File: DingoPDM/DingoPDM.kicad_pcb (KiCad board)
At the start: 4 copper layers, 71.1 x 88.9 mm, 112 parts, among them J1 RedCubeTerminal, J2 RedCubeTerminal, J3 Conn_01x12, J4 TC, U1 VXO780x-500-M, U11 BTS7008-2EPA, U12 BTS724G, U2 LD1117S33CTR, U3 PCA82C250, U4 STM32F303CCTx, U5 MB85RC256V, U6 MCP9808, U7 LM324, U8 BTS700n-1EPP, U9 BTS700n-1EPP, Y1 8mHz

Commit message: Added documentation, finished and cleaned design
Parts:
- moved G1 61.4 mm to (30.0, 32.4)
- moved TP1 23.4 mm to (-34.2, -15.6)
- moved H3 11.9 mm to (-21.1, -21.6)
- moved J2 8.33 mm to (-30.5, -23.9)
- moved C7 1.17 mm to (0.97, 49.3)
- moved C8 1.12 mm to (4.67, 49.3)
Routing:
- net GND: track 51.7 -> 72.2 mm, vias 50 -> 52
- net +5V: track 171.8 -> 157.9 mm
- net INPUT2: track 43.1 -> 46.3 mm
- net INPUT1: track 39.9 -> 41.6 mm
- net PF_IN5: track 112.2 -> 113.5 mm
- net PF_ST5_6: track 110.7 -> 111.6 mm
- added copper zone on In1.Cu, net GND
- removed copper zone on In2.Cu, net GND
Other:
- board size 71.1 x 88.9 mm -> 71.1 x 82.5 mm

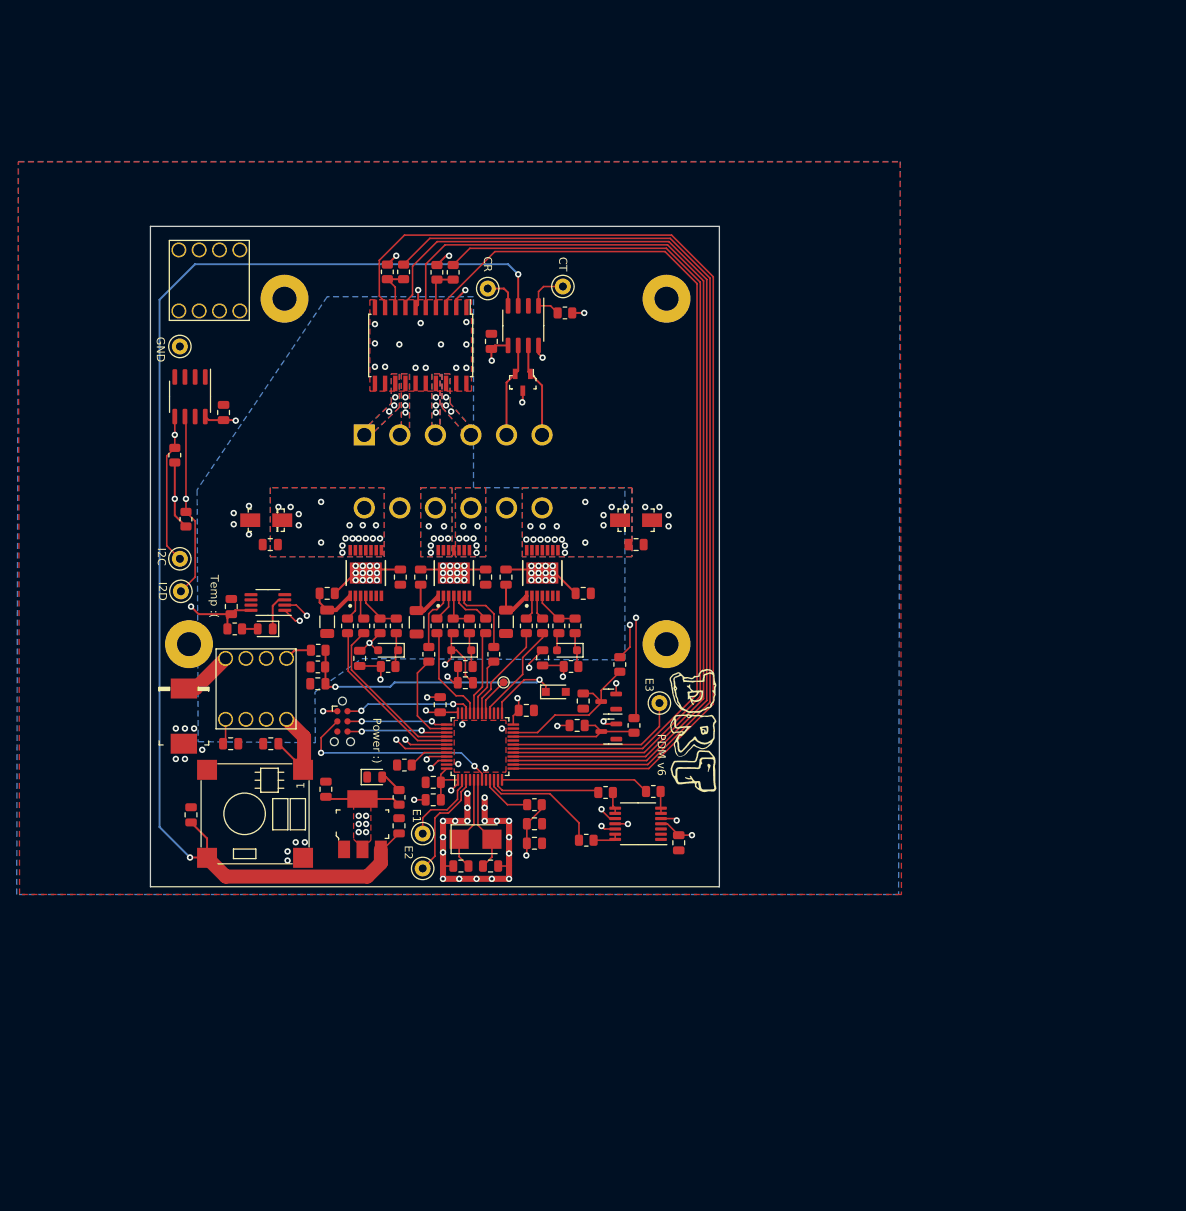
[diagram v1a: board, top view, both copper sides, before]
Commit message: Changed to STM32F446RE
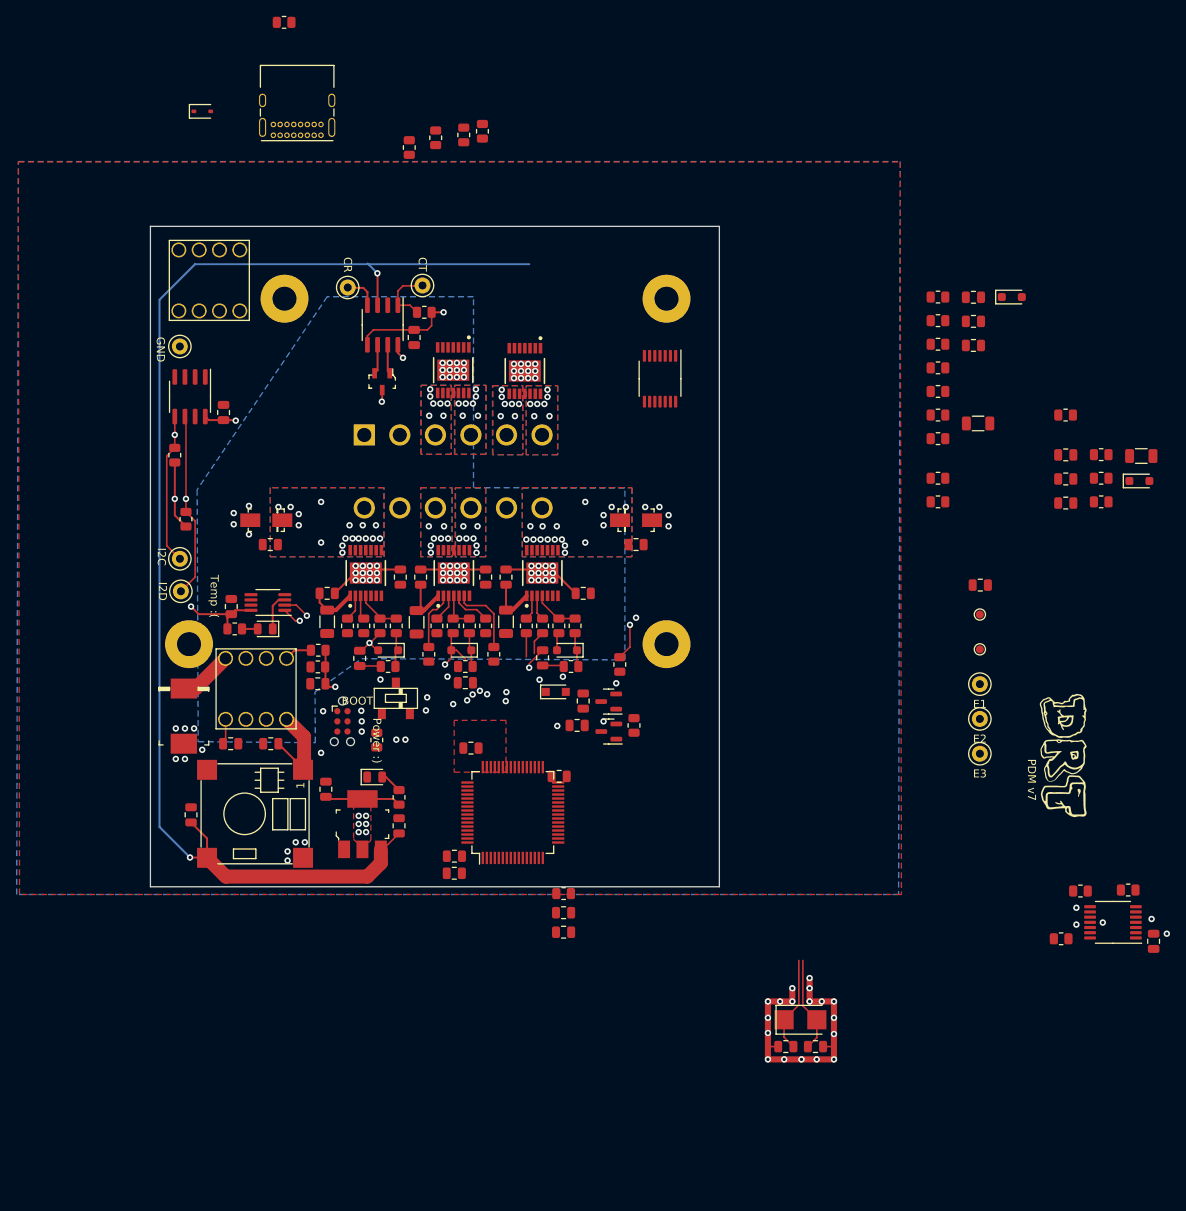
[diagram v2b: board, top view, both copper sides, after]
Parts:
- added C10: 47nF, Capacitor_SMD:C_0805_2012Metric, F.Cu at (76.6, -2.07)
- added C33: 100nF, Capacitor_SMD:C_0805_2012Metric, F.Cu at (76.6, 0.94)
- added C34: 220pF, Capacitor_SMD:C_0805_2012Metric, F.Cu at (76.6, 3.95)
- added C35: 47nF, Capacitor_SMD:C_0805_2012Metric, F.Cu at (65.0, -21.8)
- added C36: 100nF, Capacitor_SMD:C_0805_2012Metric, F.Cu at (65.0, -18.8)
- added C37: 220pF, Capacitor_SMD:C_0805_2012Metric, F.Cu at (65.0, -15.7)
- added C38: 4.7uF, Capacitor_SMD:C_0805_2012Metric, F.Cu at (65.9, 14.2)
- added D13: 3.3V, Diode_SMD:D_SOD-323_HandSoldering, F.Cu at (85.8, 1.19)
- added D14: 3.3V, Diode_SMD:D_SOD-323_HandSoldering, F.Cu at (69.8, -21.8)
- added D15: Schottky, Diode_SMD:D_SOD-323, F.Cu at (-31.4, -45.0)
- added J5: USB_C_Receptacle_USB2.0, Connector_USB:USB_C_Receptacle_GCT_USB4085, F.Cu at (-16.5, -42.0)
- added R38: 1.2k, Resistor_SMD:R_0805_2012Metric, F.Cu at (81.0, -2.10)
- added R39: 47R 1/4W, Resistor_SMD:R_1206_3216Metric, F.Cu at (86.0, -1.93)
- added R40: 4.7k, Resistor_SMD:R_0805_2012Metric, F.Cu at (81.0, 0.85)
- added R41: 4.7k, Resistor_SMD:R_0805_2012Metric, F.Cu at (81.0, 3.80)
- added R42: 1.2k, Resistor_SMD:R_0805_2012Metric, F.Cu at (60.6, 0.85)
- added R43: 4.7k, Resistor_SMD:R_0805_2012Metric, F.Cu at (60.6, -21.8)
- added R44: 4.7k, Resistor_SMD:R_0805_2012Metric, F.Cu at (60.6, -18.8)
- added R45: 4.7k, Resistor_SMD:R_0805_2012Metric, F.Cu at (60.6, -15.9)
- added R46: 4.7k, Resistor_SMD:R_0805_2012Metric, F.Cu at (60.6, -12.9)
- added R47: 1.2k, Resistor_SMD:R_0805_2012Metric, F.Cu at (60.6, -10.00)
- added R48: 47R 1/4W, Resistor_SMD:R_1206_3216Metric, F.Cu at (65.6, -6.00)
- added R49: 4.7k, Resistor_SMD:R_0805_2012Metric, F.Cu at (60.6, -7.05)
- added R50: 4.7k, Resistor_SMD:R_0805_2012Metric, F.Cu at (60.6, -4.10)
- added R51: 1.2k, Resistor_SMD:R_0805_2012Metric, F.Cu at (60.6, 3.80)
- added R56: 33K, Resistor_SMD:R_0805_2012Metric, F.Cu at (-21.1, -56.1)
- added R57: 82K, Resistor_SMD:R_0805_2012Metric, F.Cu at (76.6, -7.05)
- added SW1: BOOT, SlideSwitch:CJS-1200TB, F.Cu at (-7.16, 28.4)
- added TP10: E3, TestPoint:TestPoint_Keystone_5000-5004_Miniature, F.Cu at (65.8, 35.3)
- added U10: BTS7008-2EPA, Profet:TDSO-14, F.Cu at (8.96, -12.6)
- added U13: BTS7008-2EPA, Profet:TDSO-14, F.Cu at (0.01, -12.7)
- R17, R23, R32: value 4.7K -> 4.7k
- R8: value 100R -> 120R
- TP4: value MCO -> MCO1
- TP7: value E1 -> MCO2; footprint TestPoint:TestPoint_Keystone_5000-5004_Miniature -> TestPoint:TestPoint_Pad_D1.0mm
- TP8: value E2 -> E1
- TP9: value E3 -> E2
- U12: value BTS724G -> LM324; footprint Package_SO:Infineon_PG-DSO-20-32 -> Package_SO:TSSOP-14_4.4x5mm_P0.65mm
- U4: value STM32F303CCTx -> STM32F446RETx; footprint Package_QFP:LQFP-48_7x7mm_P0.5mm -> Package_QFP:LQFP-64_10x10mm_P0.5mm
- moved TP7 73.4 mm to (65.8, 22.2)
- moved TP8 73.4 mm to (65.8, 26.6)
- moved R25 60.6 mm to (78.4, 52.5)
- moved R11 60.6 mm to (84.4, 52.3)
- moved C21 60.6 mm to (87.6, 58.7)
- moved R12 60.6 mm to (76.0, 58.4)
- moved U7 60.6 mm to (82.5, 56.4)
- moved TP4 60.1 mm to (65.8, 17.9)
- moved C8 46.5 mm to (45.3, 71.9)
- moved Y1 46.5 mm to (43.4, 68.5)
- moved C7 46.5 mm to (41.6, 71.9)
- moved G1 46.4 mm to (76.3, 35.5)
- moved TP9 40.1 mm to (65.8, 30.9)
- moved U12 30.2 mm to (25.9, -11.6)
- moved R36 18.0 mm to (3.66, -42.5)
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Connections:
- J3 pad 1: PF_OUT8 -> CAN_L
- J3 pad 2: PF_OUT7 -> CAN_H
- J3 pad 3: PF_OUT6 -> PF_OUT8
- J3 pad 4: PF_OUT5 -> PF_OUT7
- J3 pad 5: CAN_L -> PF_OUT6
- J3 pad 6: CAN_H -> PF_OUT5
- R34 pad 1: Net-(U12-ST3/4) -> Net-(U10-IN0)
- R34 pad 2: PF_ST7_8 -> PF_IN5
- R35 pad 1: +3V3 -> Net-(U10-DEN)
- R35 pad 2: Net-(U12-ST3/4) -> PF_DEN5_6
- R36 pad 1: Net-(U12-ST1/2) -> PF_DSEL5_6
- R36 pad 2: PF_ST5_6 -> Net-(U10-DSEL)
- R37 pad 1: +3V3 -> Net-(U10-IN1)
- R37 pad 2: Net-(U12-ST1/2) -> PF_IN6
- R4 pad 1: Net-(U4-BOOT0) -> Net-(SW1-B)
- R4 pad 2: GND -> Net-(U4-BOOT0)
- TP7 pad 1: Net-(U4-PC13) -> Net-(U4-PC9)
- TP8 pad 1: Net-(U4-PC14) -> Net-(U4-PC10)
- TP9 pad 1: Net-(U4-PB1) -> Net-(U4-PC11)
- U12 pad 1: +12V -> Net-(U12A--)
- U12 pad 10: +12V -> (no net)
- U12 pad 11: +12V -> (no net)
- U12 pad 12: +12V -> (no net)
- U12 pad 13: PF_OUT8 -> (no net)
- U12 pad 14: PF_OUT7 -> (no net)
- U12 pad 2: GND -> Net-(U12A--)
- U12 pad 3: PF_IN5 -> /MedCurrentDrivers/Sheet5F5A9675/IS
- U12 pad 4: Net-(U12-ST1/2) -> (no net)
- U12 pad 5: PF_IN6 -> /MedCurrentDrivers/Sheet5F5A9676/IS
- U12 pad 6: GND -> Net-(U12B--)
- U12 pad 7: PF_IN7 -> Net-(U12B--)
- U12 pad 8: Net-(U12-ST3/4) -> (no net)
- U12 pad 9: PF_IN8 -> (no net)
- U4 pad 12: PF_IS1 -> GND
- U4 pad 13: PF_IN8 -> Net-(U4-VDDA)
- U4 pad 14: PF_ST7_8 -> PF_IS1
- U4 pad 15: PF_IN7 -> PF_IS5_6
- U4 pad 16: PF_IN6 -> PF_IS7_8
- U4 pad 17: PF_ST5_6 -> /MCU/BATT_SENSE
- U4 pad 18: PF_IN5 -> GND
- U4 pad 19: Net-(U4-PB1) -> +3V3
- U4 pad 20: unconnected-(U4-PB2-Pad20) -> PF_IN8
- U4 pad 21: IN_1 -> PF_DSEL7_8
- U4 pad 22: IN_2 -> PF_DEN7_8
- U4 pad 23: GND -> PF_IN7
- U4 pad 24: +3V3 -> PF_IN6
- U4 pad 25: /MCU/BATT_SENSE -> PF_DSEL5_6
- U4 pad 26: unconnected-(U4-PB13-Pad26) -> PF_DEN5_6
- U4 pad 27: unconnected-(U4-PB14-Pad27) -> PF_IN5
- U4 pad 29: Net-(U4-PA8) -> PF_IN1
- U4 pad 3: Net-(U4-PC14) -> unconnected-(U4-PC14-Pad3)
- U4 pad 30: PF_IN1 -> Net-(U4-VCAP_1)
- U4 pad 31: PF_IN4 -> GND
- U4 pad 32: PF_DSEL3_4 -> +3V3
- U4 pad 33: PF_DEN3_4 -> PF_IN4
- U4 pad 34: /MCU/SWDIO -> PF_DSEL3_4
- U4 pad 35: GND -> PF_DEN3_4
- U4 pad 36: +3V3 -> PF_IN3
- U4 pad 37: /MCU/SWCLK -> PF_DEN2
- U4 pad 38: PF_IN3 -> PF_IN2
- U4 pad 39: /MCU/SWO -> IN_1
- U4 pad 40: PF_DEN2 -> Net-(U4-PC9)
- U4 pad 41: PF_IN2 -> Net-(U4-PA8)
- U4 pad 42: I2C1_SCL -> USB_VBUS
- U4 pad 43: I2C1_SDA -> IN_2
- U4 pad 44: Net-(U4-BOOT0) -> USB_D-
- U4 pad 45: /MCU/CAN_RX -> USB_D+
- U4 pad 46: /MCU/CAN_TX -> /MCU/SWDIO
- U4 pad 8: GND -> unconnected-(U4-PC0-Pad8)
- U4 pad 9: Net-(U4-VDDA) -> unconnected-(U4-PC1-Pad9)
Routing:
- net PF_IN8: track 133.1 -> 0.00 mm
- net PF_IN7: track 125.5 -> 0.00 mm
- net PF_ST7_8: track 122.6 -> 0.00 mm
- net PF_IN6: track 122.0 -> 0.00 mm
- net PF_IN5: track 113.5 -> 0.00 mm
- net PF_ST5_6: track 111.6 -> 0.00 mm
- net /MCU/CAN_TX: track 119.8 -> 12.5 mm, vias 1 -> 0
- net /MCU/CAN_RX: track 104.5 -> 170.5 mm, vias 1 -> 0
- net /HighCurrentDrivers/sheet5F5A40BA/IS: track 46.7 -> 2.67 mm
- net /MedCurrentDrivers/Sheet5F5A9674/IS: track 37.4 -> 0.00 mm
- net /MCU/BATT_SENSE: track 40.6 -> 5.62 mm
- net /HighCurrentDrivers/sheet5F5A40B9/IS: track 31.4 -> 2.51 mm
- net +3V3: track 73.5 -> 45.1 mm, vias 21 -> 15
- net /MCU/NRST: track 26.8 -> 0.00 mm, vias 2 -> 1
- net I2C1_SDA: track 73.3 -> 48.9 mm
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- removed copper zone on F.Cu, net +12V
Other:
- board text added: "PDM v7"
- board text removed: "E1"
- board text removed: "E2"
- board text removed: "E3"
- board text removed: "PDM v6"

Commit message: Routed V7
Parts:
- removed TP4: MCO1, TestPoint:TestPoint_Pad_D1.0mm
- removed TP7: MCO2, TestPoint:TestPoint_Pad_D1.0mm
- added C39: 100nF, Capacitor_SMD:C_0805_2012Metric, F.Cu at (17.6, 46.2)
- added C40: 100nF, Capacitor_SMD:C_0805_2012Metric, F.Cu at (30.0, 45.6)
- C15: value 10nF -> 100nF
- R11, R12, R25, R42, R51: value 1.2k -> 120R
- moved G1 114.1 mm to (-32.4, 0.76)
- moved R56 110.2 mm to (-7.62, 53.2), turned to 90 degrees
- moved R57 101.8 mm to (-5.46, 53.2), turned to -90 degrees
- moved D15 99.3 mm to (-17.3, 53.3)
- moved J5 97.8 mm to (-17.1, 55.7), turned to 0 degrees
- moved D13 81.2 mm to (7.87, -21.8)
- moved R41 78.3 mm to (7.72, -23.9), turned to 180 degrees
- moved R40 76.8 mm to (6.86, -19.1), turned to -90 degrees
- moved R39 74.7 mm to (13.0, -17.3), turned to -90 degrees
- moved R38 74.1 mm to (8.89, -19.1), turned to 90 degrees
- moved C34 72.0 mm to (10.5, -24.6), turned to -90 degrees
- moved D14 70.8 mm to (-1.02, -21.8)
- moved TP10 69.4 mm to (-0.69, 54.9)
- moved C36 69.3 mm to (-4.06, -13.0), turned to -90 degrees
- moved TP8 67.9 mm to (-1.40, 36.0)
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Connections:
- C19 pad 1: IN_1 -> IN_2
- C20 pad 1: IN_2 -> IN_1
- D6 pad 3: IN_1 -> IN_2
- D7 pad 3: IN_2 -> IN_1
- R10 pad 1: IN_1 -> IN_2
- R10 pad 2: INPUT1 -> INPUT2
- R11 pad 1: Net-(U7B--) -> PF_IS1
- R11 pad 2: PF_IS1 -> Net-(U7B--)
- R12 pad 1: Net-(U7D--) -> PF_IS2
- R12 pad 2: PF_IS2 -> Net-(U7D--)
- R25 pad 1: Net-(U7C--) -> PF_IS3_4
- R25 pad 2: PF_IS3_4 -> Net-(U7C--)
- R42 pad 1: Net-(U12A--) -> PF_IS5_6
- R42 pad 2: PF_IS5_6 -> Net-(U12D--)
- R51 pad 1: Net-(U12B--) -> PF_IS7_8
- R51 pad 2: PF_IS7_8 -> Net-(U12C--)
- R9 pad 1: IN_2 -> IN_1
- R9 pad 2: INPUT2 -> INPUT1
- U12 pad 1: Net-(U12A--) -> (no net)
- U12 pad 10: (no net) -> /MedCurrentDrivers/Sheet5F5A9676/IS
- U12 pad 11: (no net) -> GND
- U12 pad 12: (no net) -> /MedCurrentDrivers/Sheet5F5A9675/IS
- U12 pad 13: (no net) -> Net-(U12D--)
- U12 pad 14: (no net) -> Net-(U12D--)
- U12 pad 2: Net-(U12A--) -> (no net)
- U12 pad 3: /MedCurrentDrivers/Sheet5F5A9675/IS -> (no net)
- U12 pad 4: (no net) -> +3V3
- U12 pad 5: /MedCurrentDrivers/Sheet5F5A9676/IS -> (no net)
- U12 pad 6: Net-(U12B--) -> (no net)
- U12 pad 7: Net-(U12B--) -> (no net)
- U12 pad 8: (no net) -> Net-(U12C--)
- U12 pad 9: (no net) -> Net-(U12C--)
- U4 pad 39: IN_1 -> IN_2
- U4 pad 40: Net-(U4-PC9) -> unconnected-(U4-PC9-Pad40)
- U4 pad 41: Net-(U4-PA8) -> unconnected-(U4-PA8-Pad41)
- U4 pad 43: IN_2 -> IN_1
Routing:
- net +3V3: track 45.1 -> 220.2 mm, vias 15 -> 17
- net PF_IN8: track 0.00 -> 118.8 mm
- net PF_DSEL7_8: track 0.00 -> 118.0 mm
- net /MedCurrentDrivers/Sheet5F5A9676/IS: track 0.00 -> 101.4 mm, vias 0 -> 2
- net /MCU/CAN_TX: track 12.5 -> 113.0 mm, vias 0 -> 1
- net /MedCurrentDrivers/Sheet5F5A9675/IS: track 0.00 -> 95.5 mm, vias 0 -> 2
- net PF_DEN7_8: track 0.00 -> 92.8 mm
- net PF_IN7: track 0.00 -> 90.7 mm
- net PF_IN6: track 0.00 -> 90.1 mm
- net PF_DSEL5_6: track 0.00 -> 88.0 mm
- net PF_DEN5_6: track 0.00 -> 85.1 mm
- net PF_IN5: track 0.00 -> 83.1 mm
- net /MCU/CAN_RX: track 170.5 -> 95.7 mm, vias 0 -> 1
- net /HighCurrentDrivers/sheet5F5A40BA/IS: track 2.67 -> 62.2 mm
- net /MedCurrentDrivers/Sheet5F5A9674/IS: track 0.00 -> 52.5 mm
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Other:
- board size 71.1 x 82.5 mm -> 72.4 x 95.2 mm

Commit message: Small edits
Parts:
- D15: footprint Diode_SMD:D_SOD-323 -> Diode_SMD:D_SOD-123
- R1: value 47k -> 47K
- R10, R13, R14, R17, R18, R19, R20, R23, R24, R26, R27, R28, R29, R32, R33, R34, R35, R36, R37, R40, R41, R43, R44, R45, R46, R49, R50, R9: value 4.7k -> 4.7K
- R15, R21, R30, R38, R47: value 1.2k -> 1.2K
- R2, R4, R6, R7: value 10k -> 10K
- R5: value 1k -> 1K
- moved G2 66.7 mm to (-25.8, -7.49)
- moved R35 2.87 mm to (16.2, -22.7)
- moved D15 0.61 mm to (-17.9, 53.3)
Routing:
- net Net-(U10-DEN): track 8.50 -> 11.4 mm
- net PF_DEN5_6: track 85.1 -> 82.3 mm
- net GND: track 95.0 -> 92.3 mm, vias 56 -> 57
- net USB_D-: track 44.7 -> 43.2 mm
- net PF_OUT8: vias 7 -> 9
- net PF_OUT7: vias 7 -> 9
- net PF_OUT6: vias 7 -> 9
- net PF_OUT5: vias 7 -> 9
- net PF_OUT4: vias 7 -> 9
- net PF_OUT3: vias 7 -> 9
- net PF_OUT2: vias 17 -> 20
- net PF_OUT1: vias 17 -> 20
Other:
- board text added: "1-CANL 2-CANH 3-OUT8 4-OUT7 5-OUT6 6-OUT5 7-OUT1 9-IN1 10-OUT4 11-OUT3 11-IN2 12-OUT2"
- board text added: "12V"
